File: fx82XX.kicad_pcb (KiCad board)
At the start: 4 copper layers, 62.5 x 95.3 mm, 53 parts, among them J1 VBAT, J2 GND, J4 U1V10F5, J6 Raspberry_Pi_2_3, P1 Power Button, Q1 MMFTP3401, SW1 SW_Push, SW10 SW_Push, SW11 SW_Push, SW12 SW_Push, SW13 SW_Push, SW14 SW_Push, SW15 SW_Push, SW16 SW_Push, SW17 SW_Push, SW18 SW_Push, SW19 SW_Push, SW2 SW_Push, SW20 SW_Push, SW21 SW_Push, SW22 SW_Push, SW23 SW_Push, SW24 SW_Push, SW25 SW_Push, SW26 SW_Push, SW27 SW_Push, SW28 SW_Push, SW29 SW_Push, SW3 SW_Push, SW30 Previous, SW31 SW_Push, SW32 SW_Push, SW33 SW_Push, SW34 SW_Push, SW35 SW_Push, SW37 SW_Push, SW38 SW_Push, SW39 SW_Push, SW4 SW_Push, SW40 SW_Push, SW41 SW_Push, SW42 Home, SW43 SW_Push, SW44 SW_Push, SW45 SW_Push, SW46 SW_Push, SW47 SW_Push, SW5 SW_Push, SW6 SW_Push, SW7 SW_Push, SW8 SW_Push, SW9 SW_Push

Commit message: Change symbol references
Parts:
- renumbered J4 to J3, J6 to J4
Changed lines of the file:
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@@
   (net 15 "R8")
   (net 16 "GNDPWR")
-  (net 17 "Net-(J4-Pin_1)")
+  (net 17 "Net-(J3-Pin_1)")
   (net 18 "+5V")
   (net 19 "+BATT")
@@
     (property "ki_keywords" "raspberrypi gpio")
     (attr through_hole)
-    (fp_text reference "J6" (at 0 -2.2 180) (layer "B.SilkS")
+    (fp_text reference "J4" (at 0 -2.2 180) (layer "B.SilkS")
         (effects (font (size 1 1) (thickness 0.15)))
     )
@@
     (property "ki_keywords" "connector")
     (attr through_hole)
-    (fp_text reference "J4" (at -2.2 0.675 -90) (layer "B.SilkS")
+    (fp_text reference "J3" (at -2.2 0.675 -90) (layer "B.SilkS")
         (effects (font (size 1 1) (thickness 0.15)) (justify mirror))
     )
@@
       (stroke (width 0.1) (type solid)) (layer "B.Fab"))
     (pad "1" thru_hole rect (at 0 0) (size 1.7 1.7) (drill 1) (layers "*.Cu" "*.Mask")
-      (net 17 "Net-(J4-Pin_1)") (pinfunction "Pin_1") (pintype "passive"))
+      (net 17 "Net-(J3-Pin_1)") (pinfunction "Pin_1") (pintype "passive"))
     (pad "2" thru_hole oval (at 0 -2.54) (size 1.7 1.7) (drill 1) (layers "*.Cu" "*.Mask")
       (net 16 "GNDPWR") (pinfunction "Pin_2") (pintype "passive"))
@@
       (net 18 "+5V") (pinfunction "S") (pintype "passive"))
     (pad "3" smd rect (at 1.5 0 180) (size 1.9 0.8) (layers "B.Cu" "B.Paste" "B.Mask")
-      (net 17 "Net-(J4-Pin_1)") (pinfunction "D") (pintype "passive"))
+      (net 17 "Net-(J3-Pin_1)") (pinfunction "D") (pintype "passive"))
     (model "${KICAD6_3DMODEL_DIR}/Package_TO_SOT_SMD.3dshapes/SOT-23.wrl"
       (offset (xyz 0 0 0))

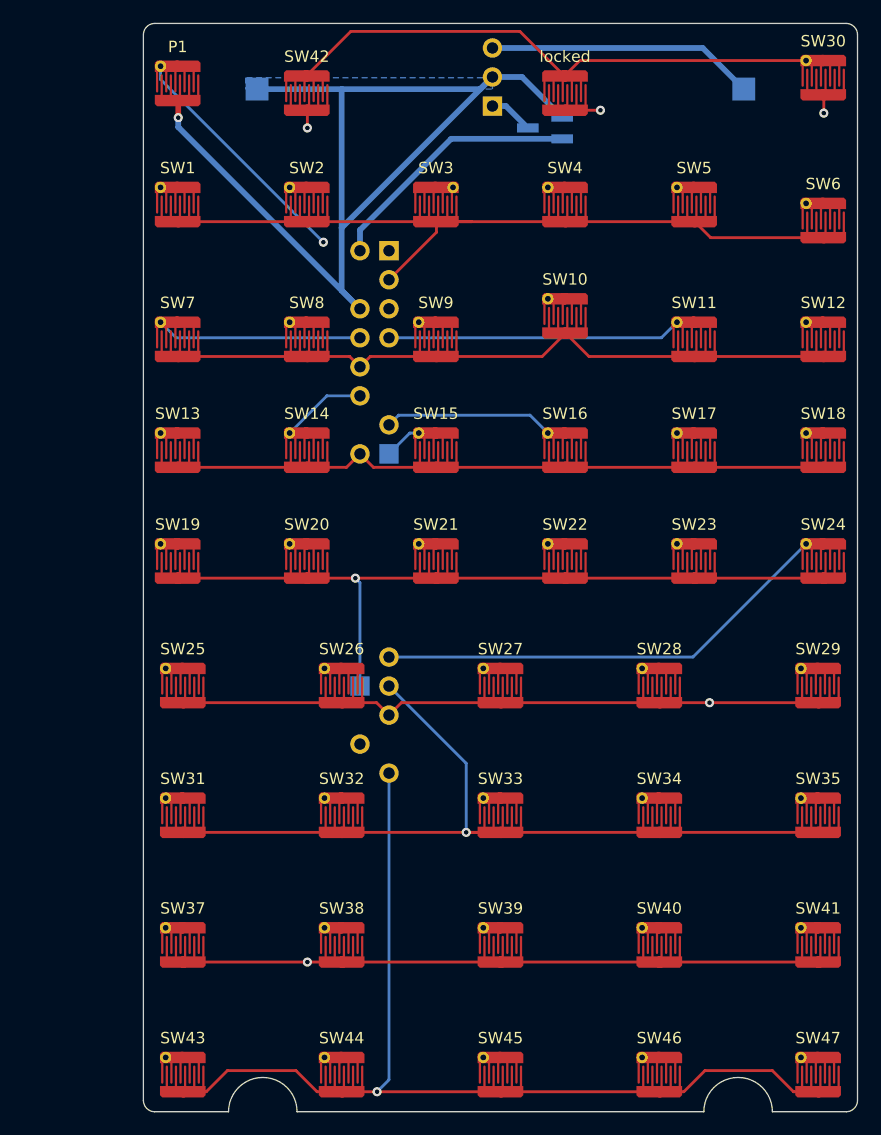
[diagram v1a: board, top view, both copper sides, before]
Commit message: Re-route using 2 layers
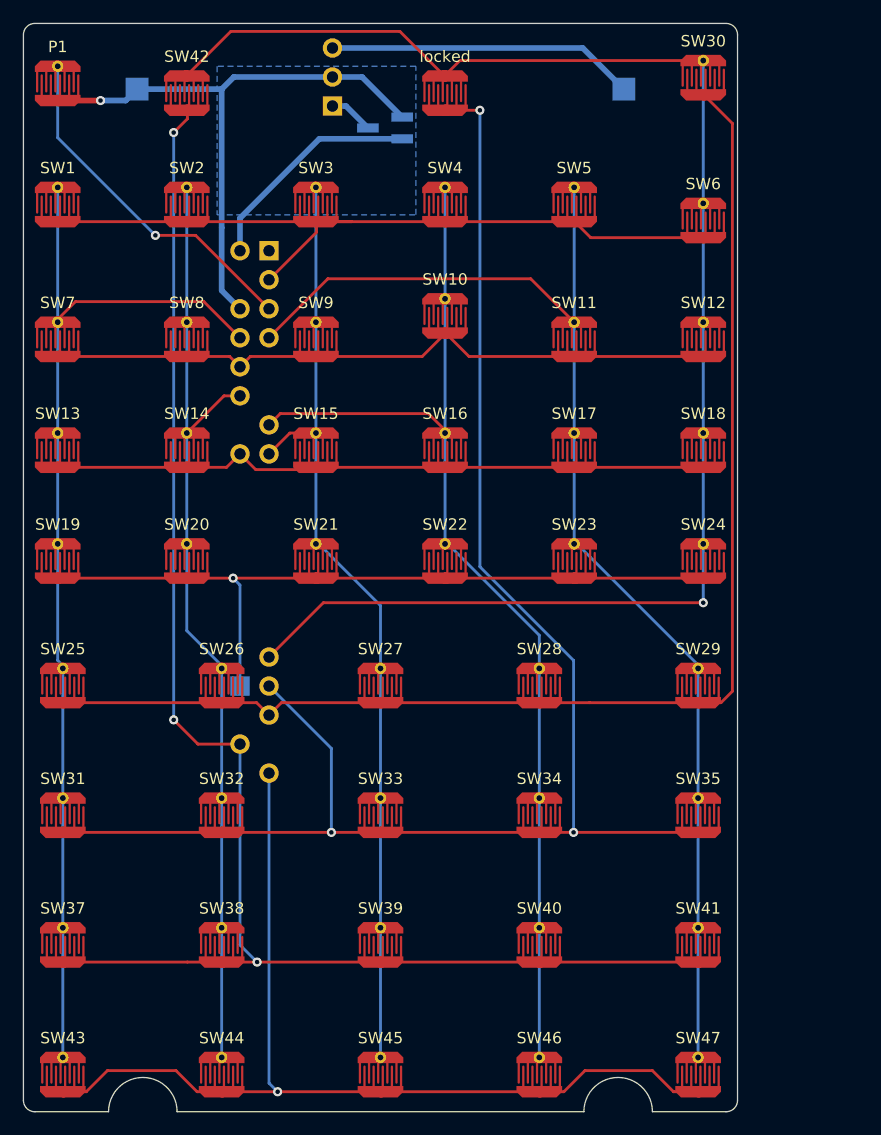
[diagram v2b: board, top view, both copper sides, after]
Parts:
- locked: value UpArrow -> Up
- moved J3 14.0 mm to (88.8, 59.5)
- moved Q1 14.0 mm to (93.4, 61.4)
- moved SW29 10.5 mm to (120.8, 110.2)
- moved SW35 10.5 mm to (120.8, 121.5)
- moved SW41 10.5 mm to (120.8, 132.9)
- moved SW47 10.5 mm to (120.8, 144.2)
- moved J1 10.5 mm to (114.3, 58.0)
- moved J2 10.5 mm to (71.7, 58.0)
- moved J4 10.5 mm to (83.2, 72.1)
- moved P1 10.5 mm to (64.8, 57.5)
- moved SW1 10.5 mm to (64.8, 68.1)
- moved SW10 10.5 mm to (98.7, 77.8)
- moved SW11 10.5 mm to (110.0, 79.9)
- moved SW12 10.5 mm to (121.2, 79.9)
- moved SW13 10.5 mm to (64.8, 89.6)
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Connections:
- net GPIO3 renamed BOOT
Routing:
- net GNDPWR: track 92.0 -> 52.3 mm
- net R6: track 145.4 -> 140.3 mm, vias 2 -> 3
- net C6: track 131.9 -> 136.7 mm, vias 0 -> 1
- net C5: track 106.4 -> 111.1 mm
- net +BATT: track 23.5 -> 27.0 mm
- net +5V: track 22.8 -> 19.9 mm
- net C4: track 94.5 -> 96.0 mm
- net C2: track 84.9 -> 83.4 mm
- net BOOT: track 29.5 -> 30.9 mm
- net R7: track 137.1 -> 135.8 mm, vias 2 -> 3
- net R5: track 113.8 -> 113.1 mm, vias 2 -> 0
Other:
- copper layers 4 -> 2

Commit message: Add holes for screws and rivets
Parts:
- added G***: LOGO, LOGO, B.Cu at (88.0, 113.0)
- moved SW37 26.0 mm to (60.2, 107.3)
- moved SW38 26.0 mm to (74.1, 107.3)
- moved SW39 26.0 mm to (88.0, 107.3)
- moved SW40 26.0 mm to (101.9, 107.3)
- moved SW41 26.0 mm to (115.8, 107.3)
- moved SW11 26.0 mm to (105.0, 54.4)
- moved SW12 26.0 mm to (116.2, 54.4)
- moved SW42 26.0 mm to (71.0, 32.8)
- moved SW7 26.0 mm to (59.8, 54.4)
- moved SW8 26.0 mm to (71.0, 54.4)
- moved SW9 26.0 mm to (82.3, 54.4)
- moved locked 26.0 mm to (93.7, 32.8)
- moved P1 26.0 mm to (59.8, 31.9)
- moved SW30 26.0 mm to (116.2, 31.4)
- moved J1 26.0 mm to (109.3, 32.5)
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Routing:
- net R8: track 86.9 -> 55.6 mm, vias 1 -> 0
- net C6: track 136.7 -> 136.1 mm
- net C5: track 111.1 -> 111.6 mm
- added copper zone on B.Cu, net (none)
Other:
- board size 62.5 x 95.3 mm -> 62.5 x 98.5 mm

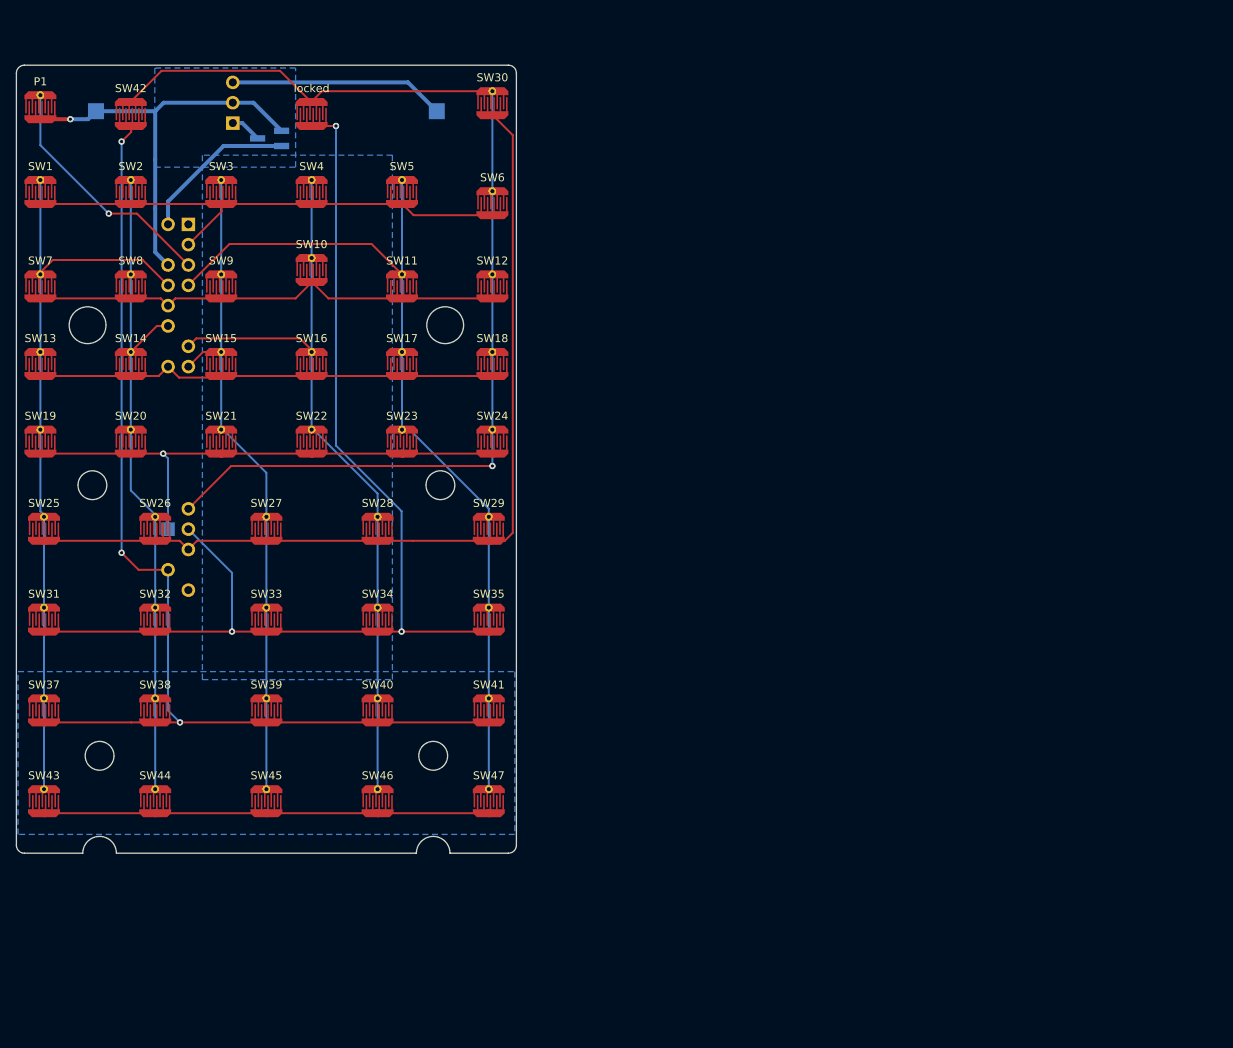
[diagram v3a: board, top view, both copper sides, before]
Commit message: Redesign PCB to be more accurate and better
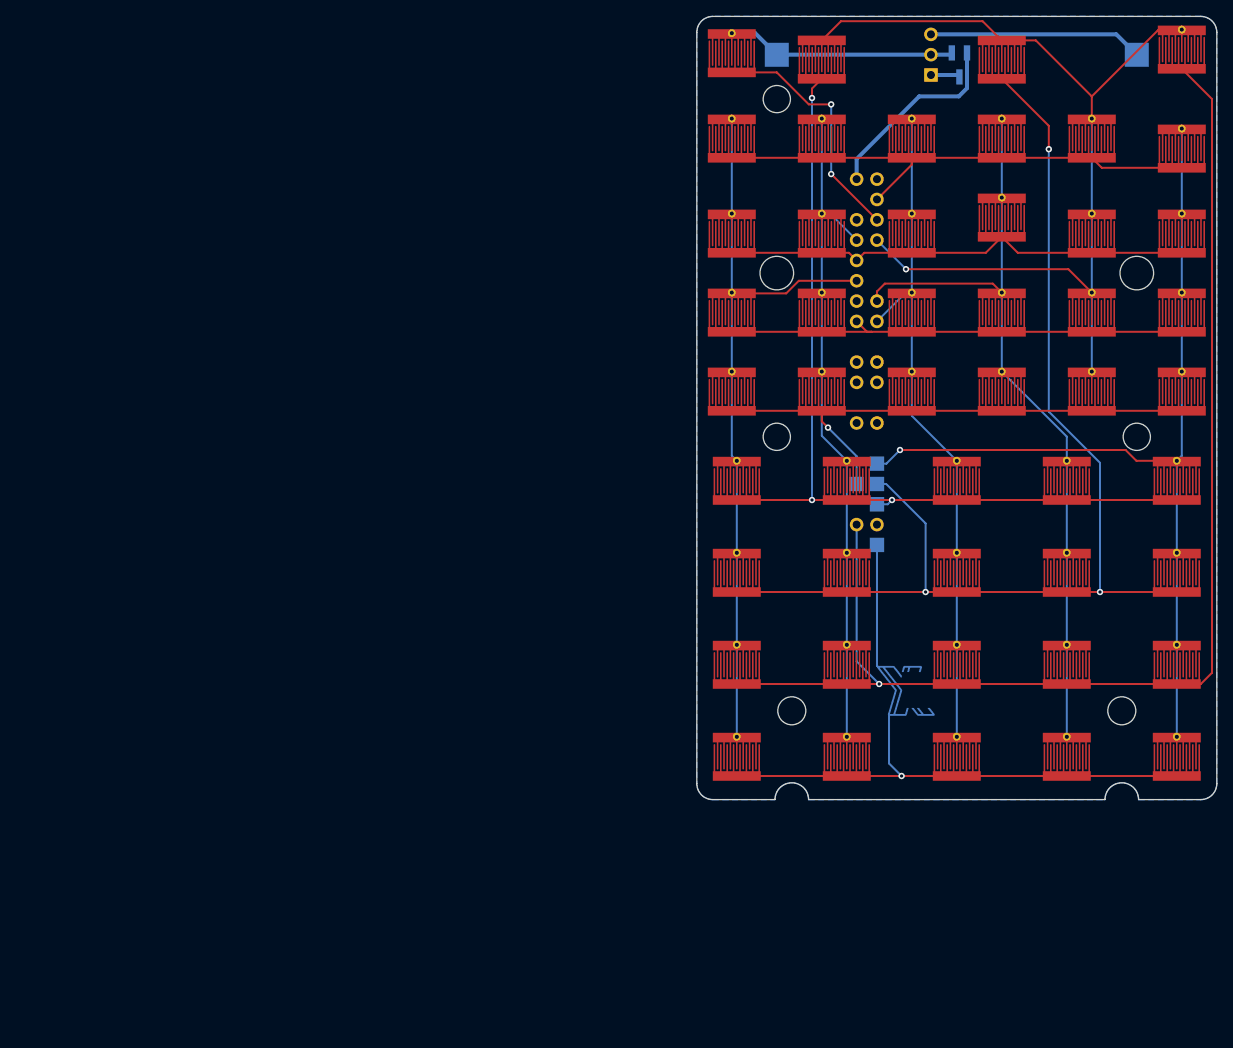
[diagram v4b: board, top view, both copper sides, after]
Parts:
- removed the G*** at (88.0, 113.0)
- added G***: fx82xx_logo, fx82:fx82xx_logo, B.Cu at (174.3, 104.9)
- +BAT: renamed from J1; footprint TestPoint:TestPoint_Pad_2.0x2.0mm -> TestPoint:TestPoint_Pad_3.0x3.0mm
- -BAT: renamed from J2; footprint TestPoint:TestPoint_Pad_2.0x2.0mm -> TestPoint:TestPoint_Pad_3.0x3.0mm
- P1: value Power Button -> On
- SW47: renamed from SW30; value Previous -> Prev
- moved +BAT 87.8 mm to (196.8, 25.4)
- moved J3 87.5 mm to (171.1, 27.9)
- moved SW25 86.8 mm to (146.8, 78.7)
- moved SW30 86.8 mm to (146.8, 90.2)
- moved SW35 86.8 mm to (146.8, 101.7)
- moved SW40 86.8 mm to (146.8, 113.2)
- moved Q1 86.7 mm to (174.6, 26.7), turned to -90 degrees
- moved P1 86.7 mm to (146.2, 25.2)
- moved SW1 86.7 mm to (146.2, 35.9)
- moved SW7 86.7 mm to (146.2, 47.8)
- moved SW13 86.7 mm to (146.2, 57.6)
- moved SW26 86.7 mm to (160.6, 78.7)
- moved SW19 86.7 mm to (146.2, 67.5)
- moved SW31 86.6 mm to (160.6, 90.2)
- moved SW45 86.6 mm to (157.4, 26.0)
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- renumbered SW31 to SW30, SW32 to SW31, SW33 to SW32, SW34 to SW33, SW35 to SW34, SW37 to SW35, SW38 to SW36, SW39 to SW37, SW40 to SW38, SW41 to SW39, SW43 to SW40, SW44 to SW41, SW45 to SW42, SW46 to SW43, SW47 to SW44, SW42 to SW45
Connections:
- J4 pad 12: C2 -> C1
- J4 pad 8: C1 -> C2
- P1 pad 1: BOOT -> GNDPWR
- P1 pad 2: GNDPWR -> BOOT
- SW29 pad 1: C5 -> C6
- SW34 pad 1: C5 -> C6
- SW39 pad 1: C5 -> C6
- SW44 pad 1: C5 -> C6
- SW45 pad 1: C6 -> C5
- SW45 pad 2: R7 -> R5
- SW47 pad 1: C6 -> C5
- SW47 pad 2: R5 -> R7
- locked pad 1: C6 -> C5
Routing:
- net GNDPWR: track 52.3 -> 28.7 mm, vias 1 -> 0
- net R8: track 55.6 -> 78.7 mm, vias 0 -> 1
- net R7: track 135.8 -> 158.1 mm, vias 3 -> 1
- net C6: track 136.1 -> 115.0 mm
- net C5: track 111.6 -> 117.3 mm, vias 0 -> 1
- net +5V: track 19.9 -> 24.4 mm
- net R1: track 67.0 -> 63.8 mm
- net R5: track 113.1 -> 110.3 mm, vias 0 -> 3
- net C4: track 96.0 -> 98.3 mm
- net C3: track 83.3 -> 85.5 mm
- net R3: track 57.6 -> 58.7 mm
- net R4: track 66.2 -> 67.2 mm
- net C2: track 83.4 -> 84.3 mm
- net R6: track 140.3 -> 140.9 mm
- net BOOT: vias 1 -> 2
- removed copper zone on B.Cu, net (none)
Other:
- board size 62.5 x 98.5 mm -> 65 x 97.9 mm

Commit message: Kicad 8.0 moment
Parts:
- renumbered locked to SW46
